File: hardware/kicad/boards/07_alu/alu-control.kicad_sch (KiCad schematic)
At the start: 18 parts, among them J7 Conn_02x05_Odd_Even, J8 Conn_02x01, SW1 SW_DIP_x04, SW14 SW_Slide_DPDT, SW15 SW_DIP_x08, U100 KM28C64A, U95 74AHC541, U96 KM28C64A, U97 74AHC541, U98 74AHC541, U99 74AHC541

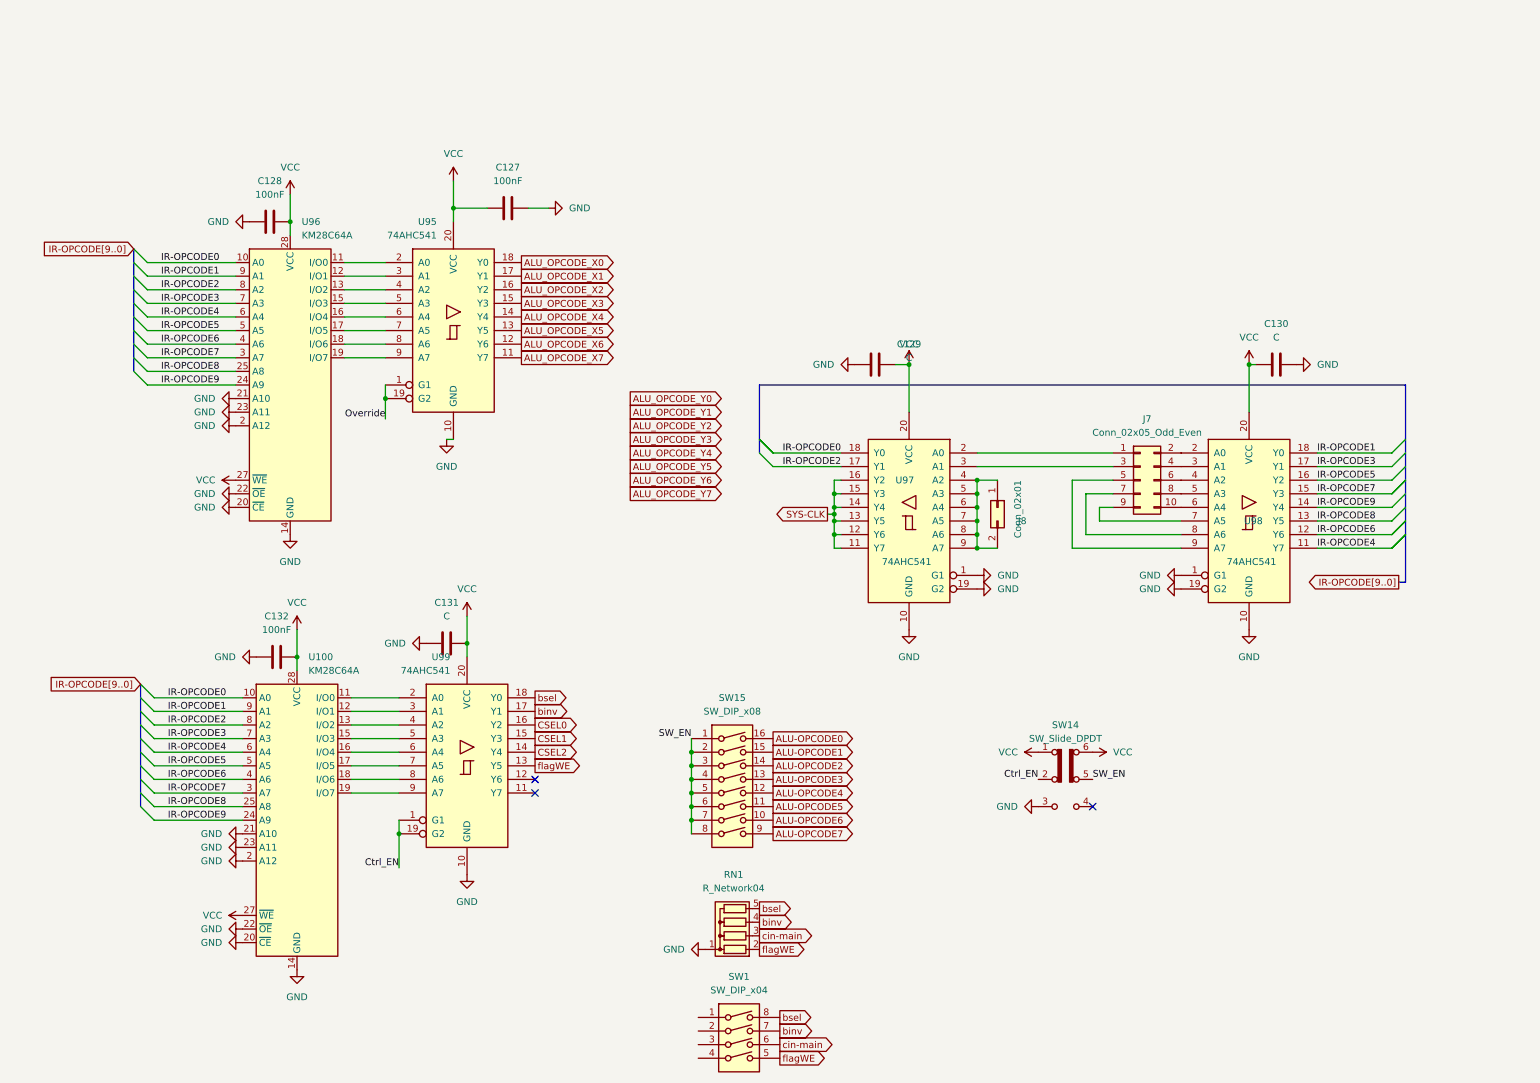
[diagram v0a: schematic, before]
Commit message: feat: implemented flag logic and led for 16 alu; refactored alu-1b cells
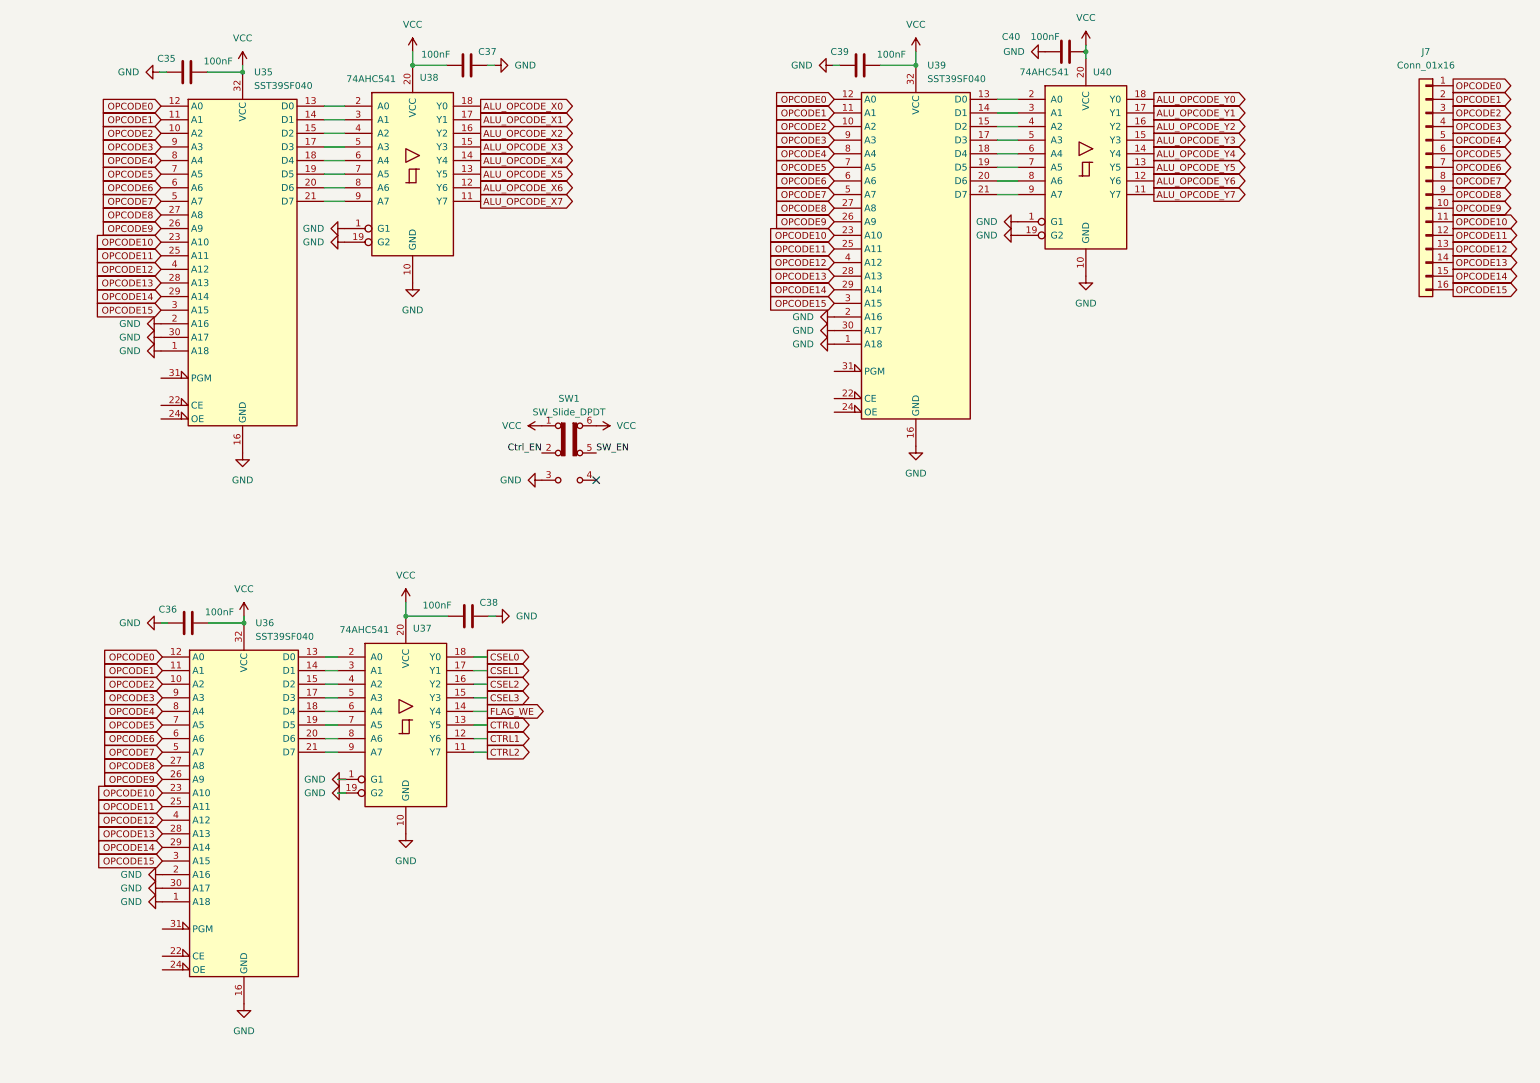
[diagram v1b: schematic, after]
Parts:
- removed C128, C132: 100nF, Capacitor_SMD:C_0603_1608Metric, symbol Device:C
- removed C129, C130: C, Capacitor_SMD:C_0603_1608Metric, symbol Device:C
- removed J7: Conn_02x05_Odd_Even, Connector_PinHeader_2.54mm:PinHeader_2x05_P2.54mm_Vertical, symbol Connector_Generic:Conn_02x05_Odd_Even
- removed J8: Conn_02x01, Connector_PinHeader_2.54mm:PinHeader_2x01_P2.54mm_Horizontal, symbol Connector_Generic:Conn_02x01
- removed RN1: R_Network04, Resistor_THT:R_Array_SIP5, symbol Device:R_Network04
- removed SW1: SW_DIP_x04, symbol Switch:SW_DIP_x04
- removed SW15: SW_DIP_x08, Button_Switch_THT:SW_DIP_SPSTx08_Slide_9.78x22.5mm_W7.62mm_P2.54mm, symbol Switch:SW_DIP_x08
- removed U100, U96: KM28C64A, Package_DIP:DIP-28_W15.24mm, symbol Memory_EEPROM:KM28C64A
- removed U97, U98: 74AHC541, Package_SO:SOIC-20W_7.5x12.8mm_P1.27mm, symbol 74xx:74AHC541
- added C35, C36, C38, C39: 100nF, Capacitor_SMD:C_0603_1608Metric, symbol Device:C
- added J7: Conn_01x16, Connector_PinHeader_2.54mm:PinHeader_1x16_P2.54mm_Vertical, symbol Connector_Generic:Conn_01x16
- added U35, U36, U39: SST39SF040, Package_DIP:DIP-32_W15.24mm, symbol Memory_Flash:SST39SF040
- added U37: 74AHC541, Package_SO:SOIC-20W_7.5x12.8mm_P1.27mm, symbol 74xx:74AHC541
- C40: renamed from C131; value C -> 100nF
- renumbered C127 to C37, SW14 to SW1, U95 to U38, U99 to U40
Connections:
- net Override is gone; now on net GND: U38.1 (G1), U38.19 (G2)
- net binv is gone; now on net ALU_OPCODE_Y1: U40.17 (Y1)
- net bsel is gone; now on net ALU_OPCODE_Y0: U40.18 (Y0)
- net flagWE is gone; now on net ALU_OPCODE_Y5: U40.13 (Y5)
- net ALU_OPCODE_Y2: now also U40.16 (Y2)
- net ALU_OPCODE_Y3: now also U40.15 (Y3)
- net ALU_OPCODE_Y4: now also U40.14 (Y4)
- net ALU_OPCODE_Y6: now also U40.12 (Y6)
- net ALU_OPCODE_Y7: now also U40.11 (Y7)
- net CSEL0: now also U37.18 (Y0); no longer U40.16 (Y2)
- net CSEL1: now also U37.17 (Y1); no longer U40.15 (Y3)
- net CSEL2: now also U37.16 (Y2); no longer U40.14 (Y4)
- net Ctrl_EN: no longer U40.1 (G1), U40.19 (G2)
- net GND: now also U40.1 (G1), U40.19 (G2), C35.2, C36.2, C38.2, C39.2, U35.1 (A18), U35.16 (GND), U35.2 (A16), U35.30 (A17), U36.1 (A18), U36.16 (GND), U36.2 (A16), U36.30 (A17), U37.1 (G1), U37.10 (GND), U37.19 (G2), U39.1 (A18), U39.16 (GND), U39.2 (A16), U39.30 (A17)
- net VCC: now also C35.1, C36.1, C38.1, C39.1, U35.32 (VCC), U36.32 (VCC), U37.20 (VCC), U39.32 (VCC)
- net at U38.2 (A0): now also U35.13 (D0)
- net at U38.3 (A1): now also U35.14 (D1)
- net at U38.4 (A2): now also U35.15 (D2)
- net at U38.5 (A3): now also U35.17 (D3)
- net at U38.6 (A4): now also U35.18 (D4)
- net at U38.7 (A5): now also U35.19 (D5)
- net at U38.8 (A6): now also U35.20 (D6)
- net at U38.9 (A7): now also U35.21 (D7)
- net at U40.2 (A0): now also U39.13 (D0)
- net at U40.3 (A1): now also U39.14 (D1)
- net at U40.4 (A2): now also U39.15 (D2)
- net at U40.5 (A3): now also U39.17 (D3)
- net at U40.6 (A4): now also U39.18 (D4)
- net at U40.7 (A5): now also U39.19 (D5)
- net at U40.8 (A6): now also U39.20 (D6)
- net at U40.9 (A7): now also U39.21 (D7)
- new net: U36.13 (D0), U37.2 (A0)
- new net: U36.14 (D1), U37.3 (A1)
- new net: U36.15 (D2), U37.4 (A2)
- new net: U36.17 (D3), U37.5 (A3)
- new net: U36.18 (D4), U37.6 (A4)
- new net: U36.19 (D5), U37.7 (A5)
- new net: U36.20 (D6), U37.8 (A6)
- new net: U36.21 (D7), U37.9 (A7)
- new net CSEL3: U37.15 (Y3)
- new net CTRL0: U37.13 (Y5)
- new net CTRL1: U37.12 (Y6)
- new net CTRL2: U37.11 (Y7)
- new net FLAG_WE: U37.14 (Y4)
- new net OPCODE0: J7.1 (Pin_1), U35.12 (A0), U36.12 (A0), U39.12 (A0)
- new net OPCODE1: J7.2 (Pin_2), U35.11 (A1), U36.11 (A1), U39.11 (A1)
- new net OPCODE10: J7.11 (Pin_11), U35.23 (A10), U36.23 (A10), U39.23 (A10)
- new net OPCODE11: J7.12 (Pin_12), U35.25 (A11), U36.25 (A11), U39.25 (A11)
- new net OPCODE12: J7.13 (Pin_13), U35.4 (A12), U36.4 (A12), U39.4 (A12)
- new net OPCODE13: J7.14 (Pin_14), U35.28 (A13), U36.28 (A13), U39.28 (A13)
- new net OPCODE14: J7.15 (Pin_15), U35.29 (A14), U36.29 (A14), U39.29 (A14)
- new net OPCODE15: J7.16 (Pin_16), U35.3 (A15), U36.3 (A15), U39.3 (A15)
- new net OPCODE2: J7.3 (Pin_3), U35.10 (A2), U36.10 (A2), U39.10 (A2)
- new net OPCODE3: J7.4 (Pin_4), U35.9 (A3), U36.9 (A3), U39.9 (A3)
- new net OPCODE4: J7.5 (Pin_5), U35.8 (A4), U36.8 (A4), U39.8 (A4)
- new net OPCODE5: J7.6 (Pin_6), U35.7 (A5), U36.7 (A5), U39.7 (A5)
- new net OPCODE6: J7.7 (Pin_7), U35.6 (A6), U36.6 (A6), U39.6 (A6)
- new net OPCODE7: J7.8 (Pin_8), U35.5 (A7), U36.5 (A7), U39.5 (A7)
- new net OPCODE8: J7.9 (Pin_9), U35.27 (A8), U36.27 (A8), U39.27 (A8)
- new net OPCODE9: J7.10 (Pin_10), U35.26 (A9), U36.26 (A9), U39.26 (A9)
- no-connect marks 3 -> 1
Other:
- moved on the sheet: C37, C40, SW1, U38, U40
